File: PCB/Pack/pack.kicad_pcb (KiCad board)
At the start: 2 copper layers, 100 x 100 mm, 76 parts, among them J1 Conn_01x01, J2 Conn_01x01, J3 Conn_01x01, J4 Conn_01x01, J5 Conn_01x01, J6 Conn_01x01, J7 Conn_01x02, J8 Conn_01x02

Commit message: minor stuff
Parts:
- removed F1, F2, F3: Fuse, Fuse_Holders_and_Fuses:Fuse_SMD1206_Wave
- moved F13 11.4 mm to (35.0, 8.00), turned to 270 degrees
- moved F19 11.4 mm to (55.0, 8.00), turned to 270 degrees
- moved F25 11.4 mm to (75.0, 8.00), turned to 270 degrees
- moved F7 11.4 mm to (15.0, 8.00), turned to 270 degrees
- moved J1 8.90 mm to (15.5, 15.0)
- moved F10 5.00 mm to (25.0, 9.00)
- moved F16 5.00 mm to (45.0, 9.00)
- moved F22 5.00 mm to (65.0, 9.00)
- moved F28 5.00 mm to (85.0, 9.00)
- moved F4 5.00 mm to (5.00, 9.00)
- moved J4 4.74 mm to (24.5, 91.0)
- moved J3 4.00 mm to (10.0, 66.0)
- moved TH1 3.26 mm to (87.8, 65.8)
- moved J7 3.25 mm to (71.0, 65.8)
- moved F31 3.16 mm to (95.0, 8.00), turned to 270 degrees
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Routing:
- net Net-(BT12-Pad2): track 120.9 -> 218.5 mm
- net Net-(BT1-Pad2): track 281.5 -> 320.5 mm
- net Net-(BT11-Pad2): track 280.4 -> 316.8 mm
- net Net-(F1-Pad1): track 42.4 -> 11.0 mm
- net Net-(BT7-Pad1): track 10.6 -> 16.7 mm
- net Net-(BT33-Pad1): track 6.26 -> 0.99 mm
- net Net-(BT25-Pad1): track 10.6 -> 15.6 mm
- net Net-(BT19-Pad1): track 10.6 -> 15.6 mm
- net Net-(BT13-Pad1): track 10.6 -> 15.6 mm
- net Net-(BT1-Pad1): track 10.6 -> 15.6 mm
- net Net-(BT32-Pad1): track 5.93 -> 0.99 mm
- net Net-(BT31-Pad1): track 3.24 -> 0.00 mm
- net Net-(J8-Pad2): track 27.1 -> 25.3 mm
- net Net-(BT22-Pad1): track 6.15 -> 5.16 mm
- net Net-(BT16-Pad1): track 6.15 -> 5.16 mm
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
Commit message: gerber
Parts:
- moved J4 1.00 mm to (24.5, 92.0)
- moved J5 0.75 mm to (50.0, 0.75), turned to 180 degrees
- moved J6 0.75 mm to (50.0, 99.2)
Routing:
- net Net-(F1-Pad1): track 11.0 -> 287.7 mm
- net Net-(BT12-Pad2): track 218.5 -> 229.7 mm
- net Net-(BT33-Pad1): track 0.99 -> 0.00 mm
- net Net-(BT32-Pad1): track 0.99 -> 0.00 mm

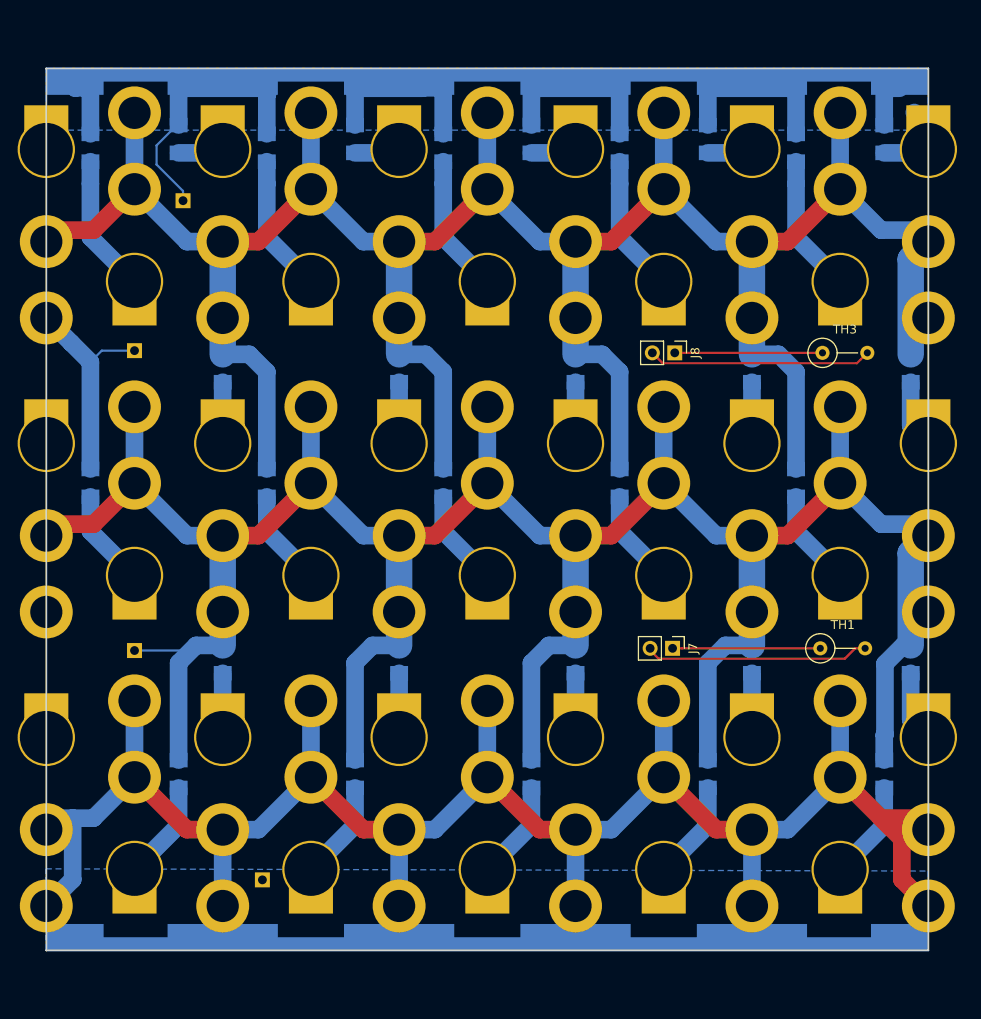
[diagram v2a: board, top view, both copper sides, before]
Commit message: no more on board fuses
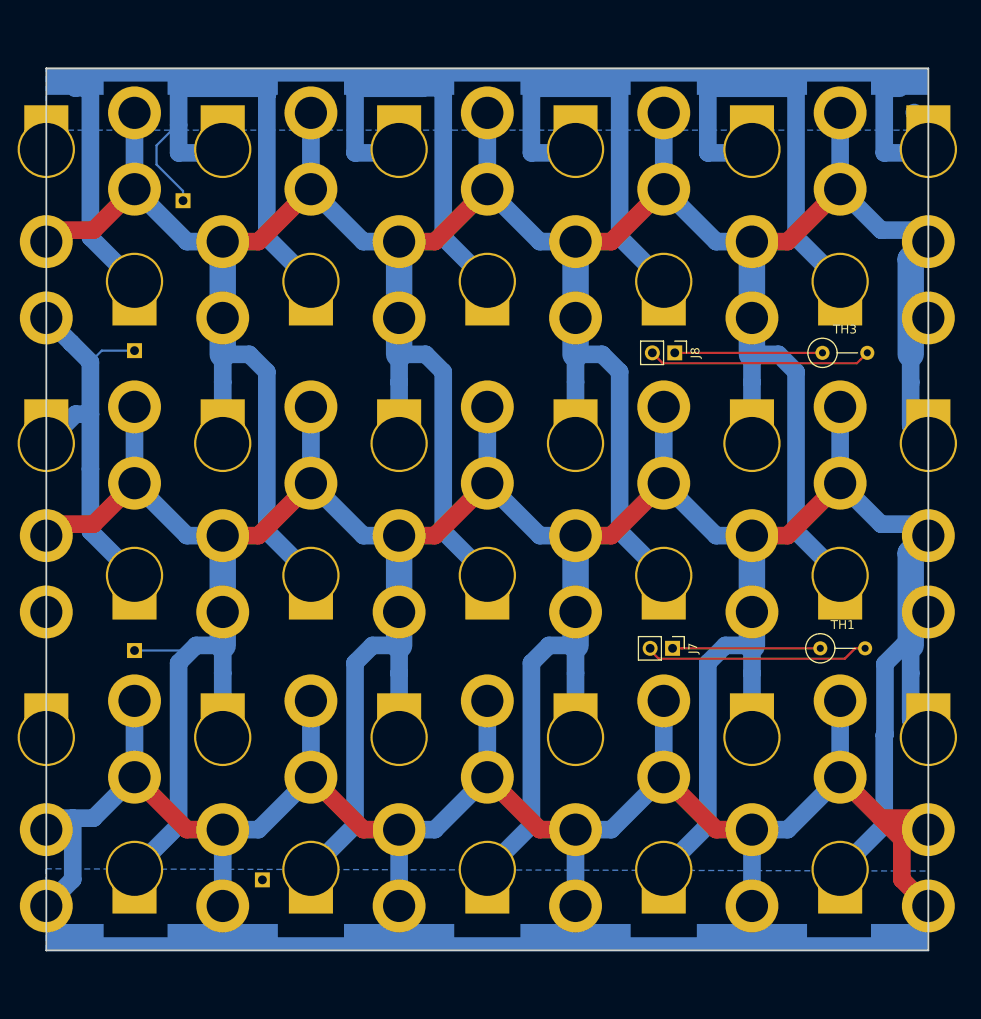
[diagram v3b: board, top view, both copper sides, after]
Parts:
- removed F10, F11, F12, F13, F14, F15, F16, F17, F18, F19, F20, F21, F22, F23, F24, F25, F26, F27, F28, F29, F30, F31, F32, F33, F4, F5, F6, F7, F8, F9: Fuse, Fuse_Holders_and_Fuses:Fuse_SMD1206_Wave
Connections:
- BT10 pad 1: Net-(BT10-Pad1) -> Net-(BT1-Pad1)
- BT11 pad 1: Net-(BT11-Pad1) -> Net-(BT1-Pad2)
- BT12 pad 1: Net-(BT12-Pad1) -> Net-(BT11-Pad2)
- BT13 pad 1: Net-(BT13-Pad1) -> Net-(BT1-Pad1)
- BT14 pad 1: Net-(BT14-Pad1) -> Net-(BT1-Pad2)
- BT15 pad 1: Net-(BT15-Pad1) -> Net-(BT11-Pad2)
- BT16 pad 1: Net-(BT16-Pad1) -> Net-(BT1-Pad1)
- BT17 pad 1: Net-(BT17-Pad1) -> Net-(BT1-Pad2)
- BT18 pad 1: Net-(BT18-Pad1) -> Net-(BT11-Pad2)
- BT19 pad 1: Net-(BT19-Pad1) -> Net-(BT1-Pad1)
- BT2 pad 1: Net-(BT2-Pad1) -> Net-(BT1-Pad2)
- BT20 pad 1: Net-(BT20-Pad1) -> Net-(BT1-Pad2)
- BT21 pad 1: Net-(BT21-Pad1) -> Net-(BT11-Pad2)
- BT22 pad 1: Net-(BT22-Pad1) -> Net-(BT1-Pad1)
- BT23 pad 1: Net-(BT23-Pad1) -> Net-(BT1-Pad2)
- BT24 pad 1: Net-(BT24-Pad1) -> Net-(BT11-Pad2)
- BT25 pad 1: Net-(BT25-Pad1) -> Net-(BT1-Pad1)
- BT26 pad 1: Net-(BT26-Pad1) -> Net-(BT1-Pad2)
- BT27 pad 1: Net-(BT27-Pad1) -> Net-(BT11-Pad2)
- BT28 pad 1: Net-(BT28-Pad1) -> Net-(BT1-Pad1)
- BT29 pad 1: Net-(BT29-Pad1) -> Net-(BT1-Pad2)
- BT3 pad 1: Net-(BT3-Pad1) -> Net-(BT11-Pad2)
- BT30 pad 1: Net-(BT30-Pad1) -> Net-(BT11-Pad2)
- BT31 pad 1: Net-(BT31-Pad1) -> Net-(BT1-Pad1)
- BT32 pad 1: Net-(BT32-Pad1) -> Net-(BT1-Pad2)
- BT33 pad 1: Net-(BT33-Pad1) -> Net-(BT11-Pad2)
- BT4 pad 1: Net-(BT4-Pad1) -> Net-(BT1-Pad1)
- BT5 pad 1: Net-(BT5-Pad1) -> Net-(BT1-Pad2)
- BT6 pad 1: Net-(BT6-Pad1) -> Net-(BT11-Pad2)
- BT7 pad 1: Net-(BT7-Pad1) -> Net-(BT1-Pad1)
- BT8 pad 1: Net-(BT8-Pad1) -> Net-(BT1-Pad2)
- BT9 pad 1: Net-(BT9-Pad1) -> Net-(BT11-Pad2)
- J1 pad 1: Net-(F1-Pad1) -> Net-(BT1-Pad1)
- J5 pad 1: Net-(F1-Pad1) -> Net-(BT1-Pad1)
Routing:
- net Net-(BT1-Pad1): track 15.6 -> 423.3 mm
- net Net-(F1-Pad1): track 287.7 -> 0.00 mm
- net Net-(BT1-Pad2): track 320.5 -> 445.1 mm
- net Net-(BT11-Pad2): track 316.8 -> 440.3 mm
- net Net-(BT7-Pad1): track 16.7 -> 0.00 mm
- net Net-(BT25-Pad1): track 15.6 -> 0.00 mm
- net Net-(BT19-Pad1): track 15.6 -> 0.00 mm
- net Net-(BT13-Pad1): track 15.6 -> 0.00 mm
- net Net-(BT9-Pad1): track 11.3 -> 0.00 mm
- net Net-(BT3-Pad1): track 11.3 -> 0.00 mm
- net Net-(BT27-Pad1): track 11.3 -> 0.00 mm
- net Net-(BT21-Pad1): track 11.3 -> 0.00 mm
- net Net-(BT15-Pad1): track 11.3 -> 0.00 mm
- net Net-(BT8-Pad1): track 11.0 -> 0.00 mm
- net Net-(BT26-Pad1): track 11.0 -> 0.00 mm
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- added copper zone on B.Cu, net Net-(BT1-Pad1)
- removed copper zone on B.Cu, net Net-(F1-Pad1)

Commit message: small change
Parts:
- BT1, BT10, BT11, BT12, BT13, BT14, BT15, BT16, BT17, BT18, BT19, BT2, BT20, BT21, BT22, BT23, BT24, BT25, BT26, BT27, BT28, BT29, BT3, BT30, BT4, BT5, BT6, BT7, BT8, BT9: footprint ENNOID:Battery -> ENNOID:18650
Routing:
- net Net-(BT1-Pad2): track 445.1 -> 0.00 mm
- net Net-(BT11-Pad2): track 440.3 -> 0.00 mm
- net Net-(BT1-Pad1): track 423.3 -> 0.00 mm
- net Net-(BT12-Pad2): track 229.7 -> 0.00 mm
- net Net-(J7-Pad2): track 25.5 -> 0.00 mm
- net Net-(J8-Pad2): track 25.3 -> 0.00 mm
- net Net-(J8-Pad1): track 16.8 -> 0.00 mm
- net Net-(J7-Pad1): track 16.8 -> 0.00 mm
- removed copper zone on B.Cu, net Net-(BT12-Pad2)
